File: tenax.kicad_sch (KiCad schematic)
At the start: 38 parts

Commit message: Last detais
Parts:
- added H1, H2: Breakaway Tabs, tenax:Breakaway_Tabs, symbol Mechanical:MountingHole
- added H10, H11, H12, H3, H4, H5, H6, H7, H8, H9: MountingHole, tenax:M2_HOLE_v2, symbol Mechanical:MountingHole
- added J1, J2: AudioJack4, tenax:MJ-4PP-9_1side, symbol Connector:AudioJack4
- SW1, SW10, SW11, SW12, SW13, SW14, SW15, SW16, SW17, SW18, SW19, SW2, SW20, SW21, SW22, SW23, SW24, SW25, SW26, SW27, SW28, SW29, SW3, SW30, SW31, SW32, SW33, SW34, SW35, SW36, SW4, SW5, SW6, SW7, SW8, SW9: renamed from SW?; footprint (none) -> tenax:CherryMX_Hotswap
- U1, U2: renamed from U?; footprint Kicad-STM32:YAAJ_WeAct_BlackPill2 -> tenax:BlackPill_STLINK
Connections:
- net k2_ 4 is gone; now on net k2_4: SW17.1 (A)
- net GND: now also U1.19 (GND), U1.39 (GND), U2.19 (GND), U2.39 (GND), J1.T, J2.T
- net k0_0: now also U1.32 (PA6)
- net k0_1: now also U1.33 (PA7); no longer SW14.1 (A), SW18.1 (A), SW26.1 (A), SW30.1 (A)
- net k0_2: now also U1.34 (PB0)
- net k0_3: now also U1.35 (PB1)
- net k0_4: now also U1.36 (PB2)
- net k0_5: now also U2.1 (PB12)
- net k0_6: now also U2.2 (PB13)
- net k0_7: now also U2.3 (PB14)
- net k0_8: now also U2.4 (PB15)
- net k0_9: now also U2.5 (PA8)
- net k1_0: now also U1.26 (PA0)
- net k1_1: now also U1.27 (PA1)
- net k1_2: now also U1.28 (PA2)
- net k1_3: now also U1.29 (PA3)
- net k1_4: now also U1.30 (PA4)
- net k1_5: now also U2.10 (PA15)
- net k1_6: now also U2.11 (PB3)
- net k1_7: now also U2.12 (PB4)
- net k1_8: now also U2.13 (PB5)
- net k1_9: now also U2.16 (PB8)
- net k2_0: now also U1.12 (PB4)
- net k2_1: now also U1.11 (PB3)
- net k2_2: now also U1.10 (PA15)
- net k2_3: now also U1.5 (PA8)
- net k2_5: now also U2.33 (PA7)
- net k2_6: now also U2.32 (PA6)
- net k2_7: now also U2.31 (PA5)
- net k2_8: now also U2.30 (PA4)
- net k2_9: now also U2.29 (PA3)
- net k3_0: now reaches U1.13 (PB5)
- net k3_0: now also SW10.1 (A)
- net TX_l: now reaches U1.14 (PB6)
- net TX_l: now also J1.R1
- net RX_l: now reaches U1.15 (PB7)
- net RX_l: now also J1.R2
- net k3_1: now reaches U1.16 (PB8)
- net k3_1: now also SW14.1 (A)
- net k3_2: now reaches U1.17 (PB9)
- net k3_2: now also SW18.1 (A)
- net +3V3: now reaches U1.20 (3V3)
- net +3V3: now also U1.37 (PB10), U1.38 (3V3), U2.20 (3V3), U2.38 (3V3), J1.S, J2.S
- net k2_4: now reaches U1.4 (PB15)
- net k3_3: now reaches SW22.1 (A)
- net k3_3: now also U2.26 (PA0)
- net TX_r: now reaches U2.14 (PB6)
- net TX_r: now also J2.R1
- net RX_r: now reaches U2.15 (PB7)
- net RX_r: now also J2.R2
- net k3_4: now reaches U2.27 (PA1)
- net k3_4: now also SW26.1 (A)
- net k3_5: now reaches U2.28 (PA2)
- net k3_5: now also SW30.1 (A)
- no-connect marks 0 -> 26
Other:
- moved on the sheet: U1, U2

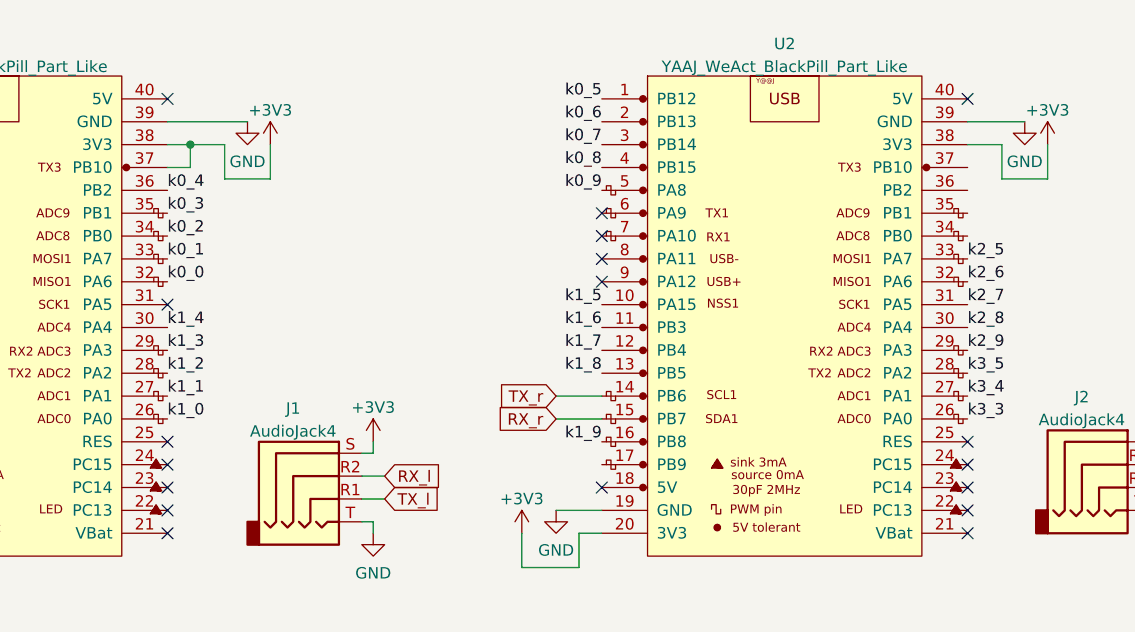
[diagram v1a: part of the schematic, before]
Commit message: production version, fixed switch connected to B2
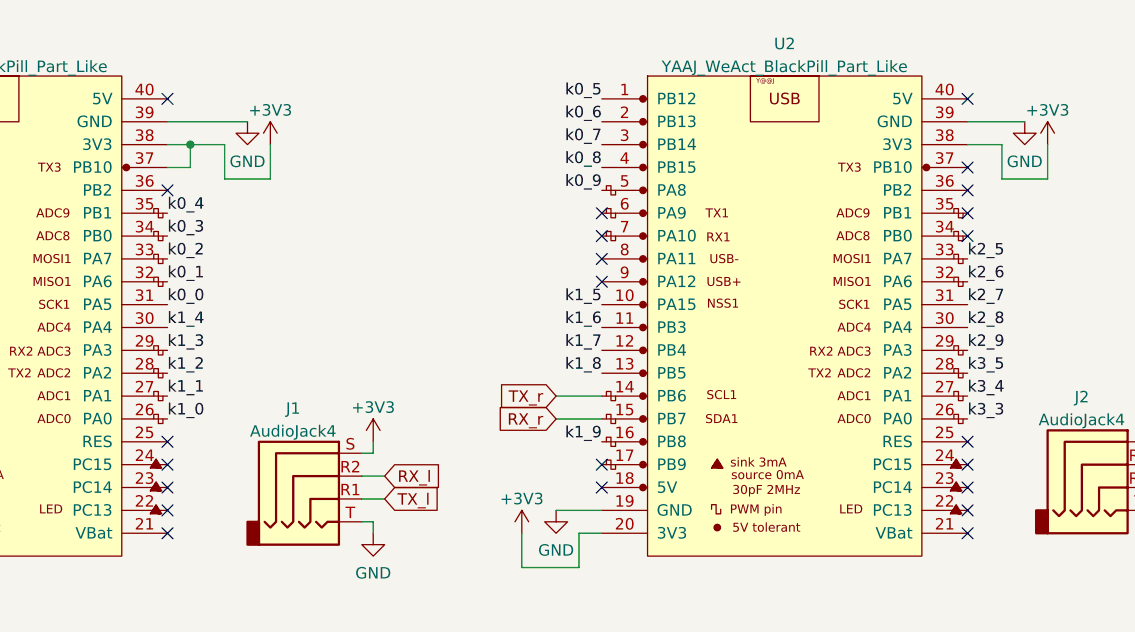
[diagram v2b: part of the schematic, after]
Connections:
- net k0_0: now also U1.31 (PA5); no longer U1.32 (PA6)
- net k0_1: now also U1.32 (PA6); no longer U1.33 (PA7)
- net k0_2: now also U1.33 (PA7); no longer U1.34 (PB0)
- net k0_3: now also U1.34 (PB0); no longer U1.35 (PB1)
- net k0_4: now also U1.35 (PB1); no longer U1.36 (PB2)
- no-connect marks 26 -> 31
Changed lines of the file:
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@@
   (junction (at 105.41 95.25) (diameter 0) (color 0 0 0 0)
   )
-  (no_connect (at 102.87 113.03))
   (no_connect (at 62.23 90.17))
   (no_connect (at 62.23 92.71))
@@
   (no_connect (at 102.87 90.17))
   (no_connect (at 62.23 133.35))
+  (no_connect (at 151.13 130.81))
+  (no_connect (at 191.77 97.79))
+  (no_connect (at 191.77 100.33))
+  (no_connect (at 191.77 102.87))
+  (no_connect (at 191.77 105.41))
+  (no_connect (at 102.87 100.33))
   (wire (pts (xy 182.88 50.8) (xy 182.88 52.07))
     (stroke (width 0) (type default) (color 0 0 0 0))
@@
     (effects (font (size 1.27 1.27)) (justify right bottom))
   )
+  (label "k0_1" (at 102.87 110.49 0)
+    (effects (font (size 1.27 1.27)) (justify left bottom))
+  )
   (label "k1_9" (at 151.13 128.27 180)
     (effects (font (size 1.27 1.27)) (justify right bottom))
@@
     (effects (font (size 1.27 1.27)) (justify right bottom))
   )
+  (label "k0_3" (at 102.87 105.41 0)
+    (effects (font (size 1.27 1.27)) (justify left bottom))
+  )
   (label "k0_3" (at 90.17 27.94 180)
     (effects (font (size 1.27 1.27)) (justify right bottom))
@@
     (effects (font (size 1.27 1.27)) (justify right bottom))
   )
-  (label "k0_2" (at 102.87 105.41 0)
-    (effects (font (size 1.27 1.27)) (justify left bottom))
-  )
   (label "k0_9" (at 205.74 27.94 180)
     (effects (font (size 1.27 1.27)) (justify right bottom))
@@
     (effects (font (size 1.27 1.27)) (justify right bottom))
   )
-  (label "k0_1" (at 102.87 107.95 0)
-    (effects (font (size 1.27 1.27)) (justify left bottom))
-  )
   (label "k2_5" (at 139.7 50.8 180)
     (effects (font (size 1.27 1.27)) (justify right bottom))
@@
     (effects (font (size 1.27 1.27)) (justify left bottom))
   )
+  (label "k0_2" (at 102.87 107.95 0)
+    (effects (font (size 1.27 1.27)) (justify left bottom))
+  )
+  (label "k0_4" (at 102.87 102.87 0)
+    (effects (font (size 1.27 1.27)) (justify left bottom))
+  )
   (label "k1_0" (at 102.87 125.73 0)
     (effects (font (size 1.27 1.27)) (justify left bottom))
@@
     (effects (font (size 1.27 1.27)) (justify right bottom))
   )
-  (label "k0_0" (at 102.87 110.49 0)
-    (effects (font (size 1.27 1.27)) (justify left bottom))
-  )
   (label "k0_4" (at 106.68 27.94 180)
     (effects (font (size 1.27 1.27)) (justify right bottom))
@@
     (effects (font (size 1.27 1.27)) (justify right bottom))
   )
-  (label "k0_4" (at 102.87 100.33 0)
-    (effects (font (size 1.27 1.27)) (justify left bottom))
-  )
   (label "k3_0" (at 73.66 62.23 180)
     (effects (font (size 1.27 1.27)) (justify right bottom))
@@
     (effects (font (size 1.27 1.27)) (justify right bottom))
   )
-  (label "k0_3" (at 102.87 102.87 0)
-    (effects (font (size 1.27 1.27)) (justify left bottom))
-  )
   (label "k3_2" (at 62.23 130.81 180)
     (effects (font (size 1.27 1.27)) (justify right bottom))
   )
+  (label "k0_0" (at 102.87 113.03 0)
+    (effects (font (size 1.27 1.27)) (justify left bottom))
+  )
   (label "k2_7" (at 191.77 113.03 0)

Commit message: fixed pcb
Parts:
- added H13, H14: Breakaway Tabs, tenax:Breakaway_Tabs, symbol Mechanical:MountingHole
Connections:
- net RX_r: now also J2.R1; no longer J2.R2
- net TX_r: now also J2.R2; no longer J2.R1
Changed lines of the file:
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@@
     )
   )
-  (global_label "TX_r" (shape input) (at 214.63 133.35 0) (fields_autoplaced)
+  (global_label "RX_r" (shape input) (at 214.63 133.35 0) (fields_autoplaced)
     (effects (font (size 1.27 1.27)) (justify left))
-    (property "Intersheet References" "${INTERSHEET_REFS}" (id 0) (at 220.9741 133.2706 0)
+    (property "Intersheet References" "${INTERSHEET_REFS}" (id 0) (at 221.2764 133.2706 0)
       (effects (font (size 1.27 1.27)) (justify left) hide)
     )
   )
-  (global_label "RX_r" (shape input) (at 214.63 130.81 0) (fields_autoplaced)
+  (global_label "TX_r" (shape input) (at 214.63 130.81 0) (fields_autoplaced)
     (effects (font (size 1.27 1.27)) (justify left))
-    (property "Intersheet References" "${INTERSHEET_REFS}" (id 0) (at 221.2764 130.7306 0)
+    (property "Intersheet References" "${INTERSHEET_REFS}" (id 0) (at 220.9741 130.7306 0)
       (effects (font (size 1.27 1.27)) (justify left) hide)
     )
@@
     (pin "1")
   )
+  (symbol (lib_id "Mechanical:MountingHole") (at 49.53 161.29 0) (unit 1)
+    (in_bom yes) (on_board yes) (fields_autoplaced)
+    (property "Reference" "H14" (id 0) (at 52.07 160.4553 0)
+      (effects (font (size 1.27 1.27)) (justify left))
+    )
+    (property "Value" "Breakaway Tabs" (id 1) (at 52.07 162.9922 0)
+      (effects (font (size 1.27 1.27)) (justify left))
+    )
+    (property "Footprint" "tenax:Breakaway_Tabs" (id 2) (at 49.53 161.29 0)
+      (effects (font (size 1.27 1.27)) hide)
+    )
+    (property "Datasheet" "~" (id 3) (at 49.53 161.29 0)
+      (effects (font (size 1.27 1.27)) hide)
+    )
+  )
   (symbol (lib_id "Switch:SW_SPST") (at 194.31 27.94 0) (unit 1)
     (in_bom yes) (on_board yes) (fields_autoplaced)
@@
     (pin "2")
   )
+  (symbol (lib_id "Mechanical:MountingHole") (at 49.53 156.21 0) (unit 1)
+    (in_bom yes) (on_board yes) (fields_autoplaced)
+    (property "Reference" "H13" (id 0) (at 52.07 155.3753 0)
+      (effects (font (size 1.27 1.27)) (justify left))
+    )
+    (property "Value" "Breakaway Tabs" (id 1) (at 52.07 157.9122 0)
+      (effects (font (size 1.27 1.27)) (justify left))
+    )
+    (property "Footprint" "tenax:Breakaway_Tabs" (id 2) (at 49.53 156.21 0)
+      (effects (font (size 1.27 1.27)) hide)
+    )
+    (property "Datasheet" "~" (id 3) (at 49.53 156.21 0)
+      (effects (font (size 1.27 1.27)) hide)
+    )
+  )
   (symbol (lib_id "Mechanical:MountingHole") (at 46.99 176.53 0) (unit 1)
     (in_bom yes) (on_board yes) (fields_autoplaced)
@@
       (reference "H12") (unit 1) (value "MountingHole") (footprint "tenax:M2_HOLE_v2")
     )
+    (path "/f3be7314-21a2-4312-9ba4-7598d6023ade"
+      (reference "H13") (unit 1) (value "Breakaway Tabs") (footprint "tenax:Breakaway_Tabs")
+    )
+    (path "/33932896-63ed-4f51-9b24-5b61ee7bf9c7"
+      (reference "H14") (unit 1) (value "Breakaway Tabs") (footprint "tenax:Breakaway_Tabs")
+    )
     (path "/7f026a8b-9cea-49b1-ba29-8183f7c510f7"
